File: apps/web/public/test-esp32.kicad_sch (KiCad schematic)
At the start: 9 parts, among them J1 USB_5V, SW1 EN_BTN, U1 ESP32-WROOM-32, U2 AMS1117-3.3

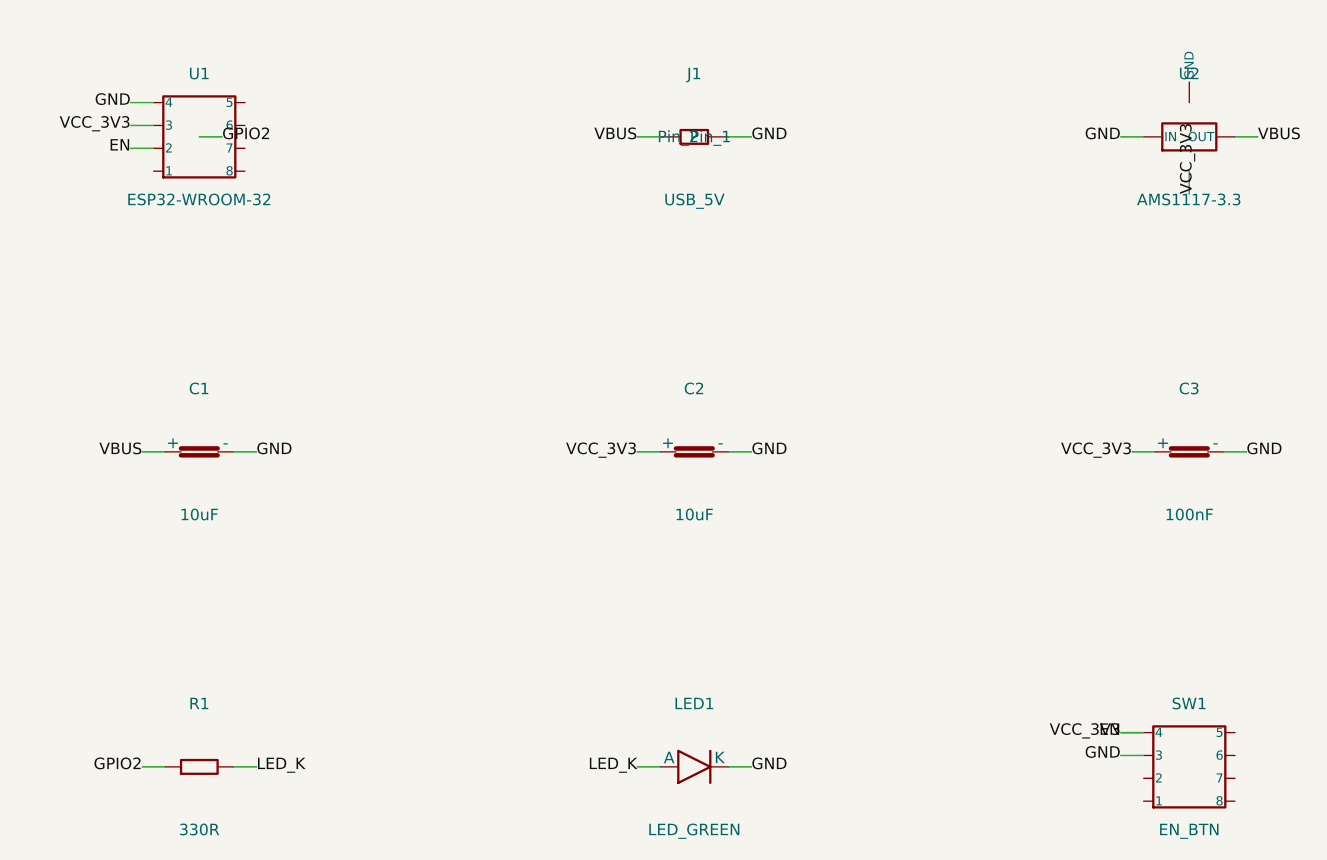
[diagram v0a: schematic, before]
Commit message: fix: remove title_h padding to eliminate empty space at bottom of schematic
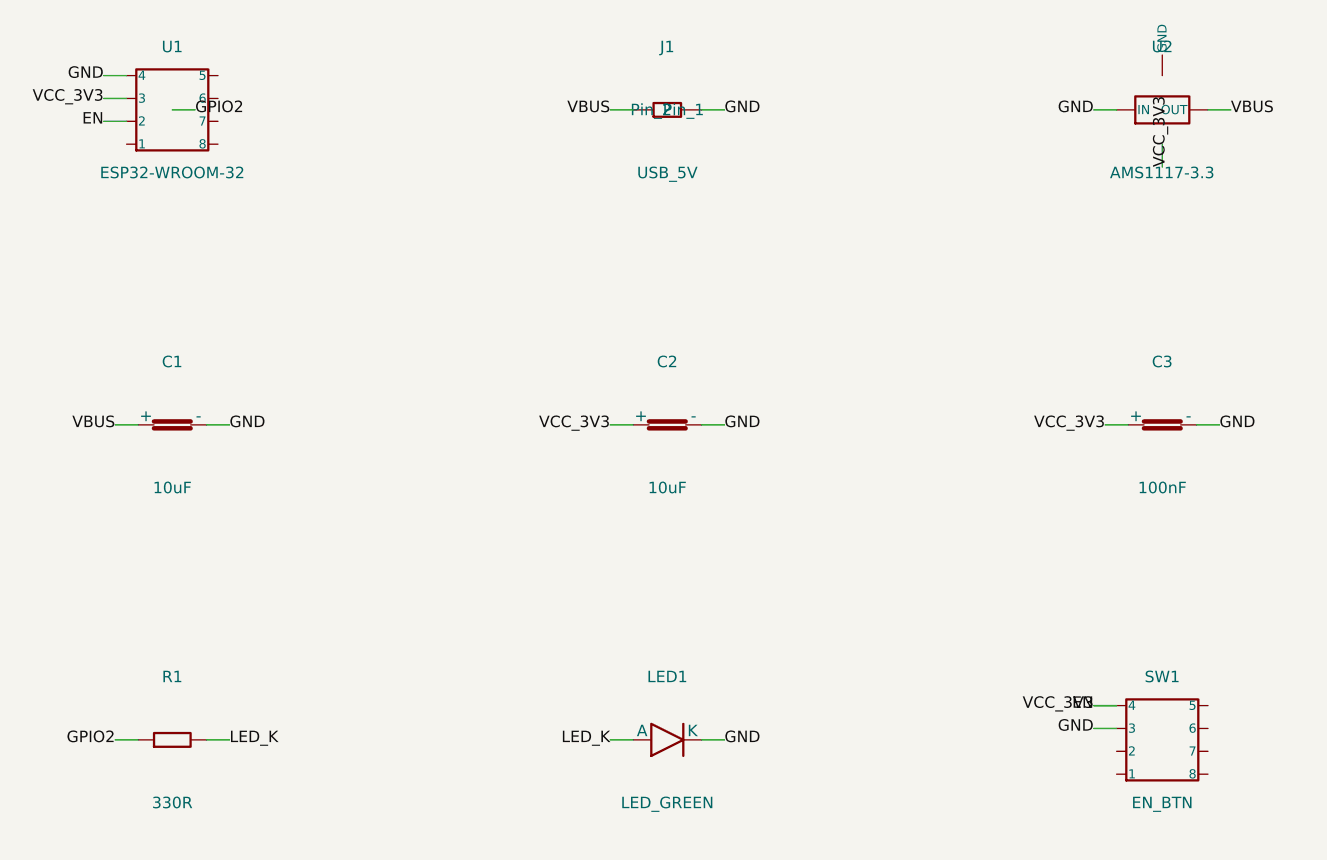
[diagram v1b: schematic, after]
